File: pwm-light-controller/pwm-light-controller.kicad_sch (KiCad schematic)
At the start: 3 parts, among them U1 AMS1117-5.0

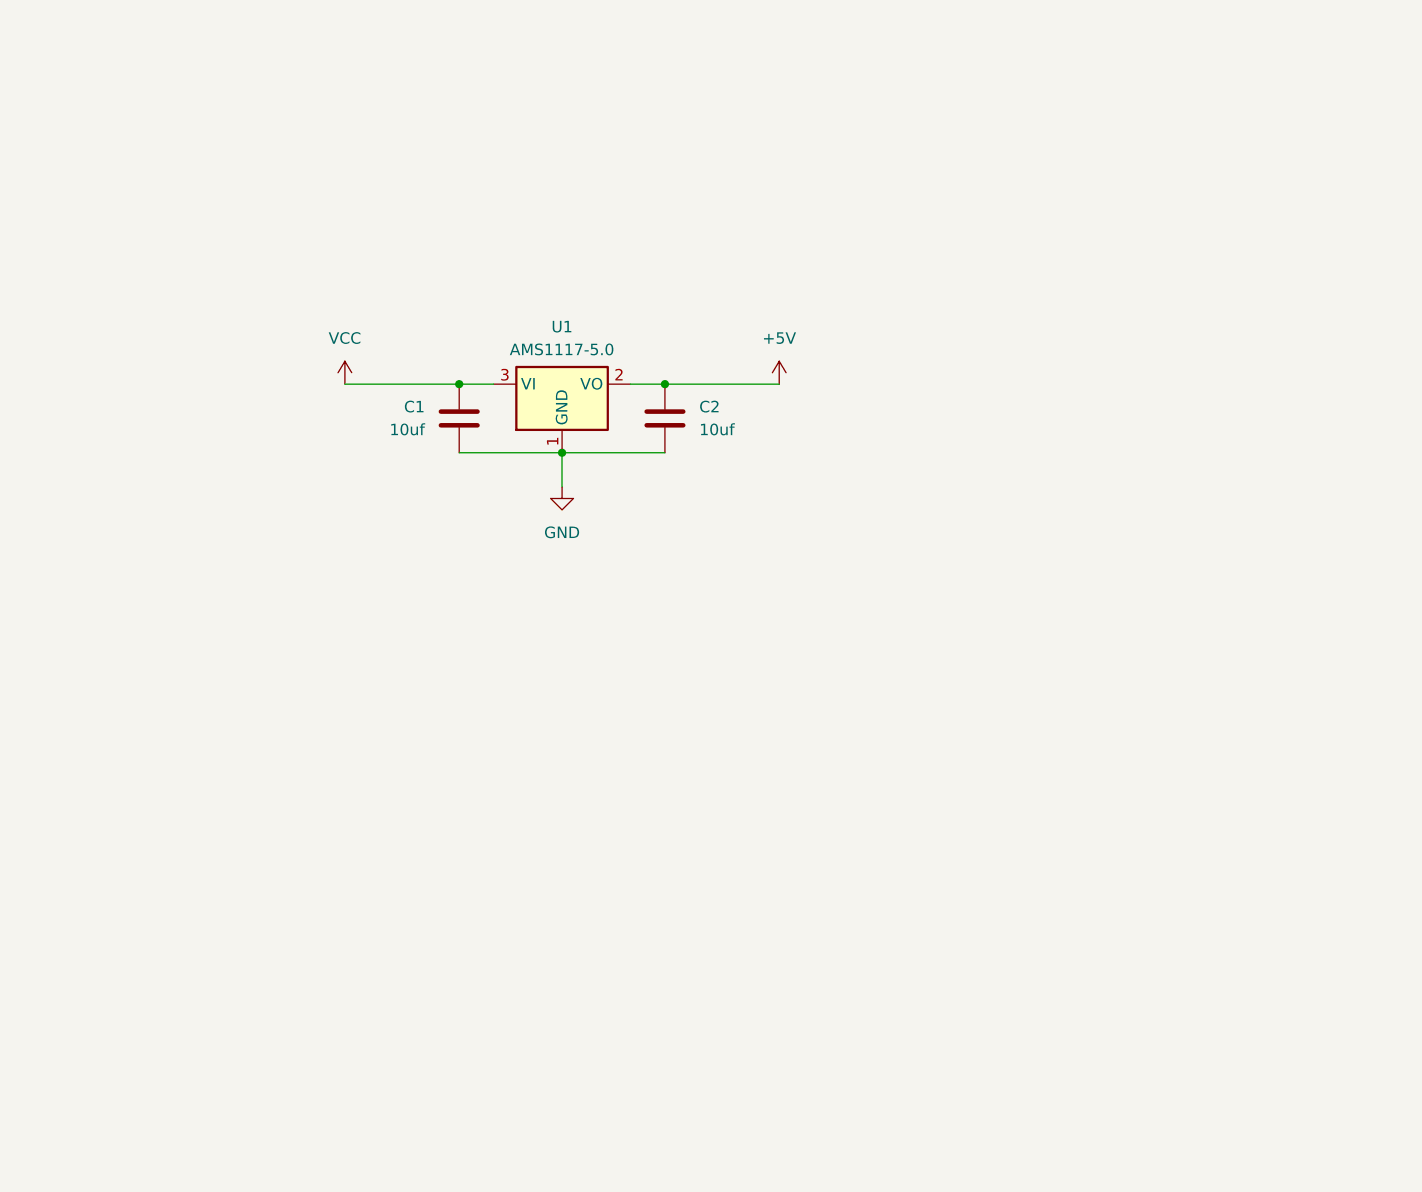
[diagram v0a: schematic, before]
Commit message: Add potentiometers and ATtiny13A
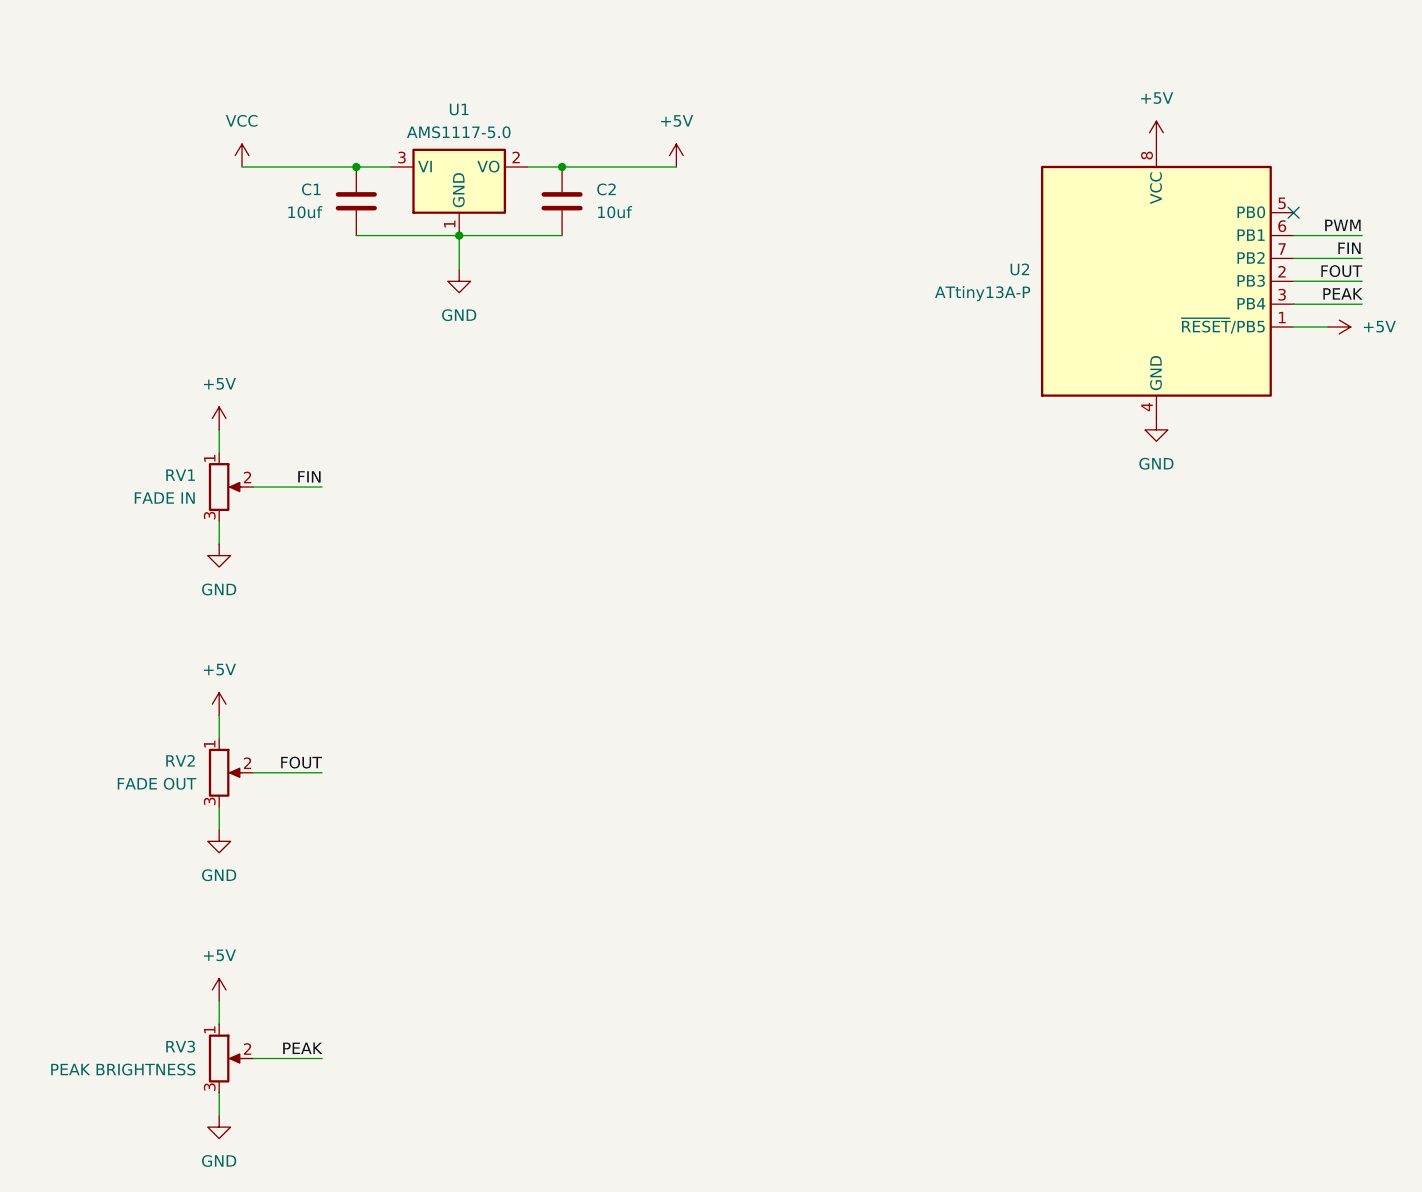
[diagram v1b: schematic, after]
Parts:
- added RV1: FADE IN, symbol Device:R_Potentiometer
- added RV2: FADE OUT, symbol Device:R_Potentiometer
- added RV3: PEAK BRIGHTNESS, symbol Device:R_Potentiometer
- added U2: ATtiny13A-P, Package_DIP:DIP-8_W7.62mm, symbol MCU_Microchip_ATtiny:ATtiny13A-P
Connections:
- net +5V: now also RV1.1, RV2.1, RV3.1, U2.1 (~{RESET}/PB5), U2.8 (VCC)
- net GND: now also RV1.3, RV2.3, RV3.3, U2.4 (GND)
- new net FIN: RV1.2, U2.7 (PB2)
- new net FOUT: RV2.2, U2.2 (PB3)
- new net PEAK: RV3.2, U2.3 (PB4)
- new net PWM: U2.6 (PB1)
- no-connect marks 0 -> 1
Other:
- moved on the sheet: C1, C2, U1

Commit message: Add header to switch peak signal
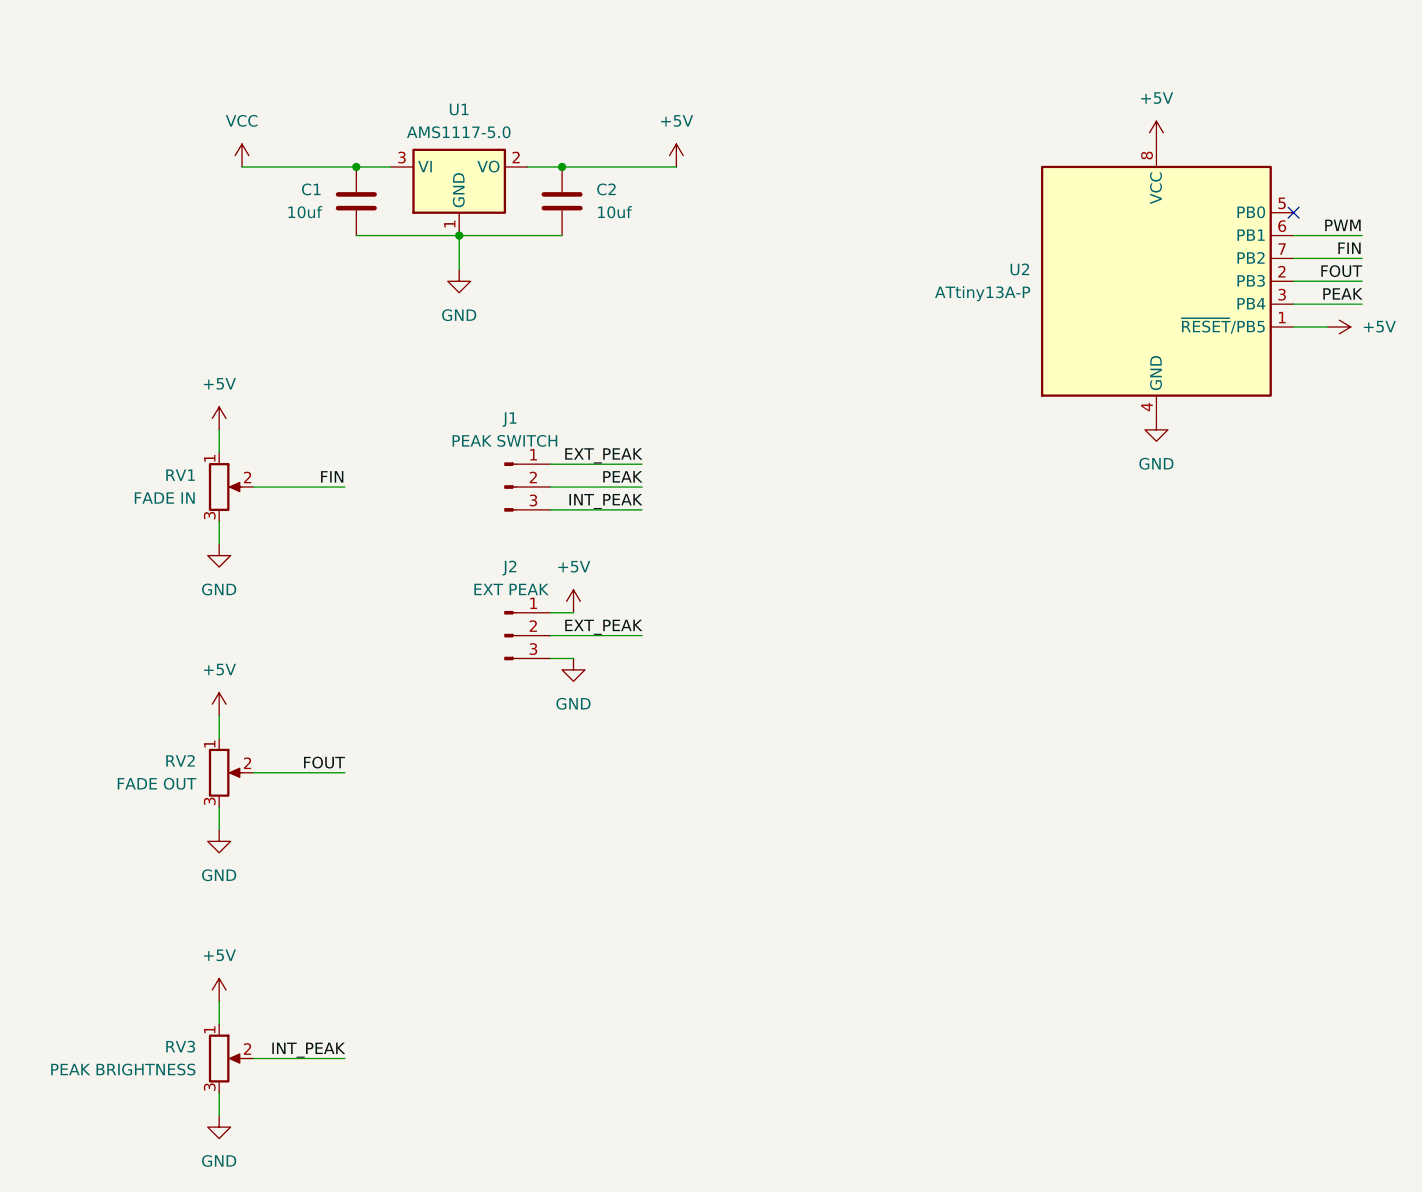
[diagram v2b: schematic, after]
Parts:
- added J1: PEAK SWITCH, symbol Connector:Conn_01x03_Pin
- added J2: EXT PEAK, symbol Connector:Conn_01x03_Pin
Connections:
- net +5V: now also J2.1 (Pin_1)
- net GND: now also J2.3 (Pin_3)
- net PEAK: now also J1.2 (Pin_2); no longer RV3.2
- new net EXT_PEAK: J1.1 (Pin_1), J2.2 (Pin_2)
- new net INT_PEAK: J1.3 (Pin_3), RV3.2

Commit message: Add headers for IO
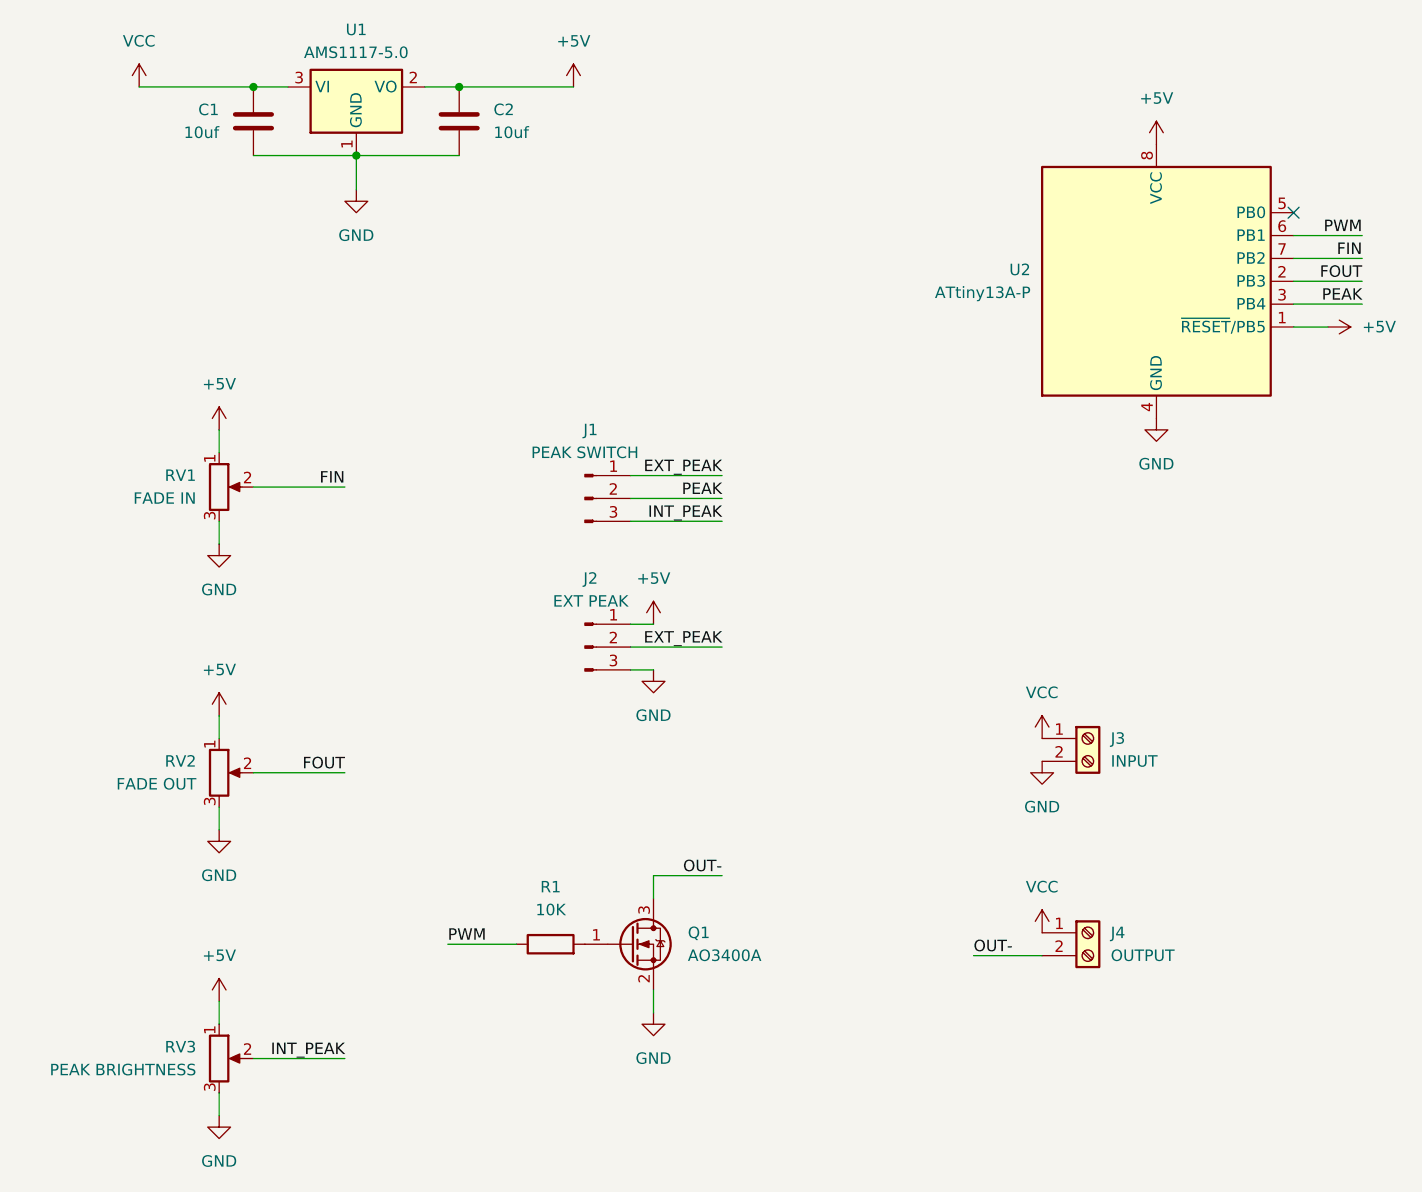
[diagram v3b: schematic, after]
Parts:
- added J3: INPUT, symbol Connector:Screw_Terminal_01x02
- added J4: OUTPUT, symbol Connector:Screw_Terminal_01x02
- added Q1: AO3400A, Package_TO_SOT_SMD:SOT-23, symbol Transistor_FET:AO3400A
- added R1: 10K, symbol Device:R
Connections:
- net GND: now also J3.2 (Pin_2), Q1.2 (S)
- net PWM: now also R1.1
- net VCC: now also J3.1 (Pin_1), J4.1 (Pin_1)
- new net: Q1.1 (G), R1.2
- new net OUT-: J4.2 (Pin_2), Q1.3 (D)
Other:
- moved on the sheet: C1, C2, J1, J2, U1
